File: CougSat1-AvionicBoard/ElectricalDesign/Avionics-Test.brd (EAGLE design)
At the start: 90.4 x 95.8 mm, 213 parts, among them J1 +X Panel GPS, J10 iFJR SD1, J11 -Y, J12 +Z, J13 +X, J14 -Z, J15 +Y, J16 IFJR SD0, J2 IHU SD1, J3 SWD, J4 CougSat Card, J5 -X, J6 IHU SD0, J8 SWD, J9 SWD, U1 STM32L476RGT, U10 BNO055, U11 M24M01, U12 TXS0102DQM, U13 TXS0102DQM, U14 AD8515, U15 BNO055, U16 BNO055, U17 TXS0102DQM, U18 TXS0102DQM, U19 AD8515, U2 STM32L476RGT, U20 INA199C2, U21 INA199C2, U22 TXS0102DQM, U23 TXS0102DQM, U24 AD8515, U25 AD7291, U26 AD7291, U27 TXS0102DQM, U28 INA199C2, U29 AD8515, U3 STM32L476RGT, U30 DRV8837, U4 M24M01, U5 TXS0102DQM, U6 DRV8837, U7 DRV8837, U8 AD7291, U9 Venus838FLPx-L, Y1 8MHz ±10ppm, Y10 32.768kHz ±10ppm, Y2 32.768kHz ±10ppm, Y3 8MHz ±10ppm, Y4 32.768kHz ±10ppm, Y5 8MHz ±10ppm, Y6 32.768kHz ±10ppm, Y7 32.768kHz ±10ppm, Y8 32.768kHz ±10ppm

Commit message: Recovered Board FIle
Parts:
- moved TP1 0.19 mm to (30.5, 39.0)
- moved C78 0.10 mm to (71.8, 15.9)
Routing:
- net 3.3V_2: track 243.0 -> 424.0 mm, vias 20 -> 43
- net COIL-Y_COIL+: track 34.5 -> 161.7 mm, vias 1 -> 3
- net COIL-Y_COIL-: track 36.7 -> 162.3 mm, vias 1 -> 2
- net CTRL_SYNC: track 5.80 -> 102.7 mm, vias 1 -> 4
- net TEMP_GPS: track 0.00 -> 92.4 mm, vias 0 -> 4
- net TEMP_PCB-3: track 2.52 -> 78.3 mm, vias 0 -> 2
- net TEMP_PCB-2: track 2.20 -> 76.1 mm, vias 0 -> 2
- net COIL-X_COIL+: track 0.00 -> 72.5 mm, vias 0 -> 1
- net COIL-Z_COIL+: track 58.9 -> 130.3 mm
- net COIL-X_COIL-: track 1.69 -> 69.1 mm, vias 0 -> 1
- net COIL-Z_COIL-: track 60.8 -> 125.9 mm
- net TEMP_H-BRIDGE-Z: track 0.09 -> 61.3 mm, vias 0 -> 2
- net TEMP_H-BRIDGE-X: track 0.00 -> 60.9 mm, vias 0 -> 4
- net TEMP_H-BRIDGE-Y: track 0.00 -> 59.3 mm, vias 0 -> 4
- net ADCS_I2C1_SCL: track 184.6 -> 243.1 mm, vias 5 -> 6
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
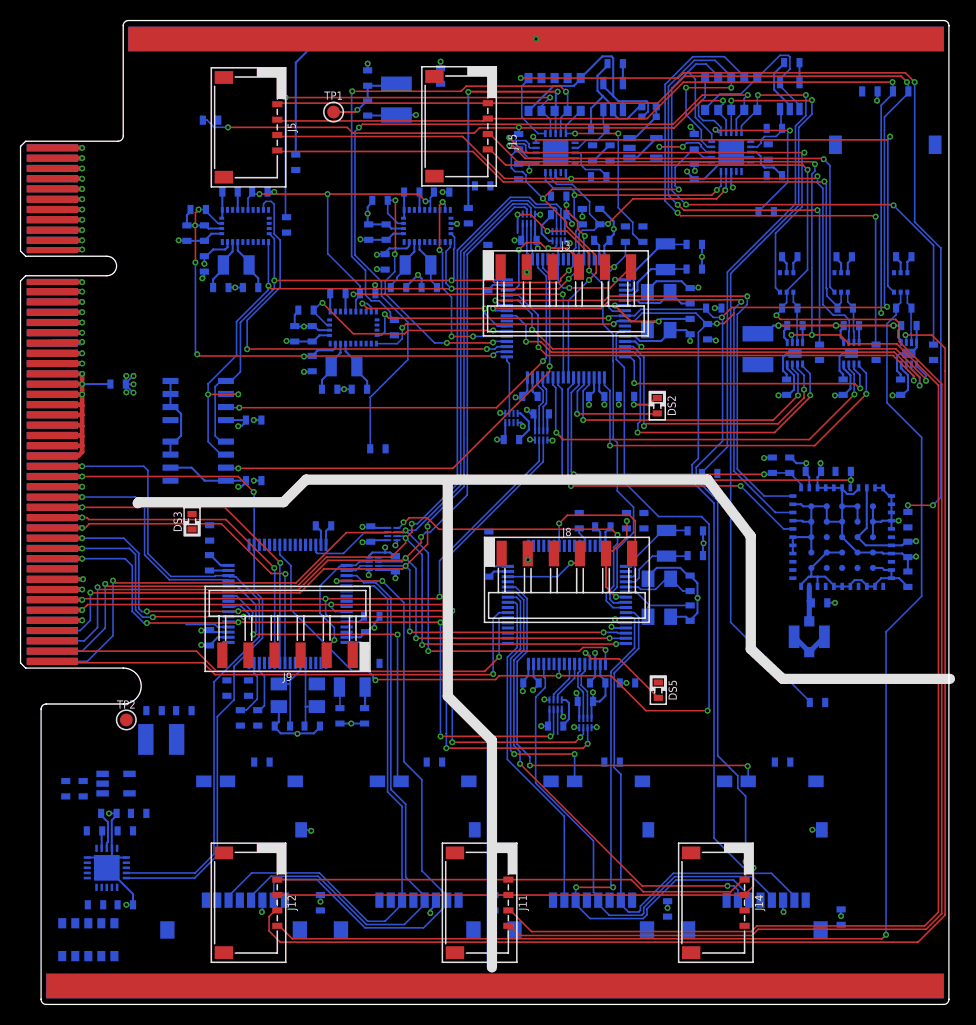
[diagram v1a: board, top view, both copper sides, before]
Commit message: Finished Routing C&DH ADC
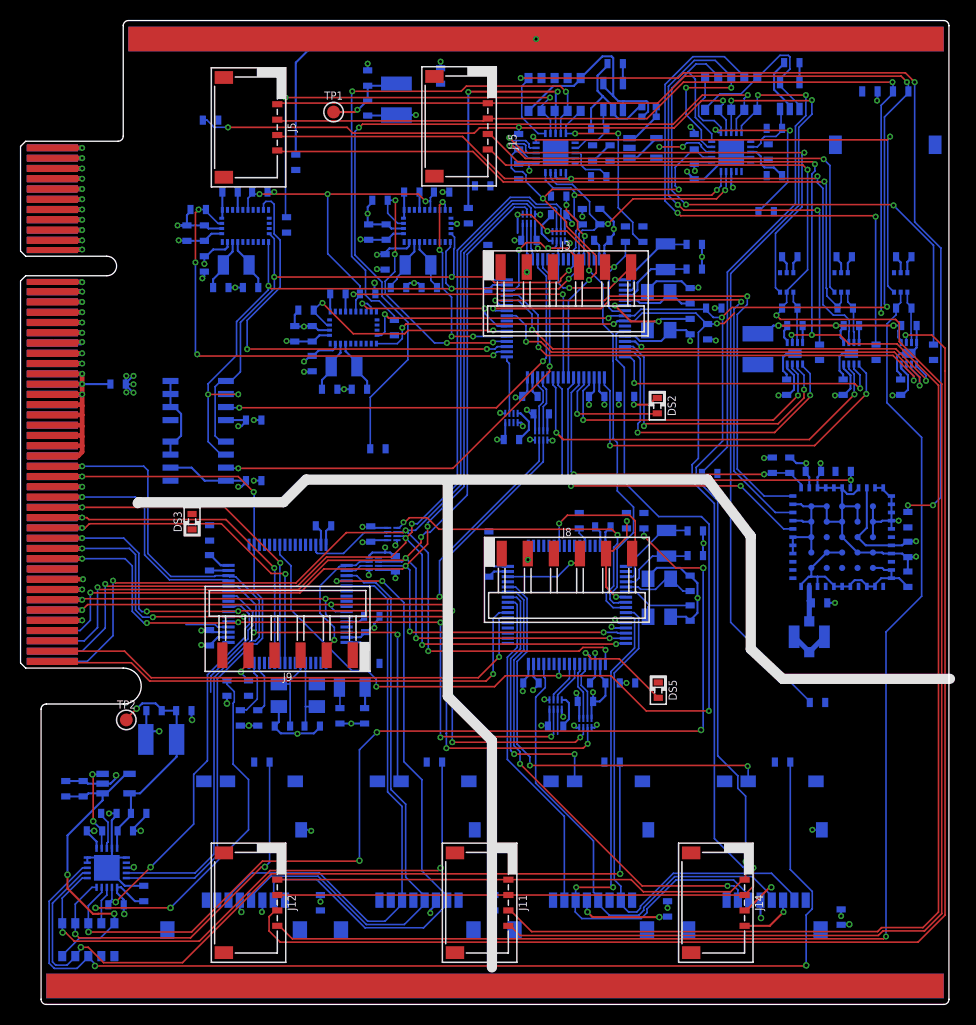
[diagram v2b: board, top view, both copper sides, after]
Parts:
- moved C15 2.11 mm to (12.0, -37.1), turned to 90 degrees
- moved R7 2.00 mm to (9.30, -38.2), turned to 180 degrees
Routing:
- net TEMP_SD_IFJR1: track 0.00 -> 107.1 mm, vias 0 -> 2
- net TEMP_IFJR: track 0.00 -> 102.9 mm, vias 0 -> 6
- net TEMP_SD_IFJR0: track 0.00 -> 81.8 mm, vias 0 -> 2
- net TEMP_SD_IHU1: track 0.00 -> 57.1 mm, vias 0 -> 2
- net DGND: track 228.9 -> 279.7 mm, vias 50 -> 49
- net 3.3V_0: track 23.8 -> 73.4 mm, vias 8 -> 13
- net AGND: track 29.0 -> 70.3 mm, vias 1 -> 6
- net 3.3V_2: track 424.0 -> 462.3 mm, vias 43 -> 44
- net TEMP_IHU: track 0.00 -> 37.8 mm, vias 0 -> 2
- net TEMP_SD_IHU0: track 0.00 -> 37.5 mm, vias 0 -> 2
- net !C&DH_ADC_RESET: track 2.87 -> 38.5 mm, vias 0 -> 2
- net AVREF-2: track 0.00 -> 30.8 mm, vias 0 -> 2
- net 3.3V_5: track 28.1 -> 58.8 mm, vias 12 -> 16
- net AVDD-1: track 0.00 -> 22.5 mm, vias 0 -> 1
- net IHU_SD_SW0: track 3.82 -> 12.5 mm
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
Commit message: Rearranged IHU GPIO for Routing
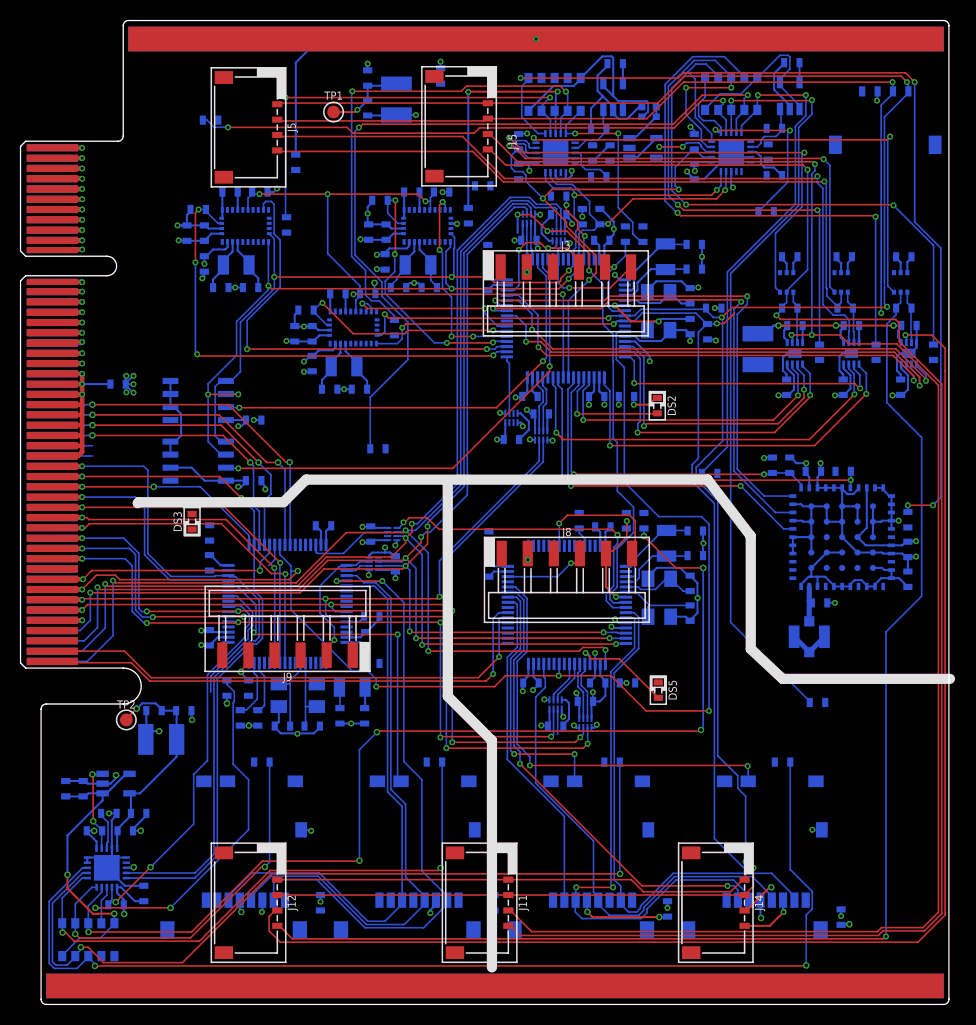
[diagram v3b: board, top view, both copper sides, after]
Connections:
- net IHU_GPIO-0: now also U3.41; no longer U3.40
- net IHU_GPIO-1: now also U3.40; no longer U3.36
- net IHU_GPIO-2: now also U3.36; no longer U3.35
- net IHU_GPIO-3: now also U3.35; no longer U3.17
- net IHU_GPIO-5: now also U3.17; no longer U3.41
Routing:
- net IHU_GPIO-0: track 0.00 -> 33.5 mm, vias 0 -> 2
- net IHU_GPIO-1: track 0.00 -> 32.2 mm, vias 0 -> 2
- net IHU_GPIO-2: track 0.00 -> 30.4 mm, vias 0 -> 2
- net IHU_GPIO-3: track 0.00 -> 28.7 mm, vias 0 -> 2
- net CTRL_SYNC: track 103.7 -> 126.4 mm, vias 4 -> 5
- net IHU_GPIO-7: track 2.98 -> 23.5 mm, vias 1 -> 2
- net BUS_I2C1_IRQ: track 5.80 -> 24.9 mm, vias 1 -> 2
- net 3.3V_2: track 462.3 -> 454.6 mm
- net IHU_GPIO-5: track 0.00 -> 3.90 mm
- net IHU_GPIO-6: track 0.00 -> 2.27 mm
- net BUS_I2C1_SCL: track 70.7 -> 69.7 mm
- net DGND: track 279.7 -> 280.0 mm, vias 49 -> 48

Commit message: Routed Some Power
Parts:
- moved DS1 57.0 mm to (83.0, 4.00), turned to 180 degrees
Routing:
- net DGND: track 280.0 -> 576.8 mm, vias 48 -> 69
- net CHASSIS: track 33.3 -> 209.9 mm, vias 1 -> 2
- net AGND: track 70.3 -> 237.7 mm, vias 6 -> 23
- net 3.3V_0: track 73.4 -> 174.5 mm, vias 13 -> 21
- net 3.3V_5: track 58.8 -> 132.1 mm, vias 16 -> 20
- net IHU_SD_CS1: track 5.19 -> 29.1 mm
- net IHU_SD_CS0: track 5.74 -> 28.0 mm
- net PGND: track 62.9 -> 77.6 mm, vias 3 -> 6
- net ADCS_I2C1_SDA: track 227.2 -> 241.7 mm
- net AVDD-0: track 19.3 -> 33.5 mm, vias 1 -> 5
- net ADCS_HALF_REF: track 3.41 -> 16.3 mm, vias 0 -> 3
- net GPS_LED_DIODE: track 0.00 -> 3.69 mm
- net 3.3V_2: track 454.6 -> 450.9 mm, vias 44 -> 43
- net IFJR_LED_GND: track 0.00 -> 2.55 mm, vias 0 -> 1
- net IFJR_SWD_VSENSE: track 0.00 -> 1.89 mm, vias 0 -> 1
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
